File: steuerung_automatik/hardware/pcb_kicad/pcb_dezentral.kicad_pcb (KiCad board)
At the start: 2 copper layers, 55 x 73.5 mm, 84 parts, among them J1 1146810000, J2 1146900000, J901 USB_C_Receptacle_USB2.0, Q1 AO3400A, SW1 dip_switch_SPST16, SW901 SW_MEC_5E, U1 SP3485EN-L/TR, U2 AOZ1282CI, U901 RP2040, U902 AMS1117-3.3, U903 W25Q128JVS, Y901 Crystal_GND24_Small

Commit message: Testpunkte
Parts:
- added D26: LED RED, 00_project_library:LED_0603_1608Metric, F.Cu at (80.3, 99.1)
- added IO18: TestPoint, TestPoint:TestPoint_Pad_D1.0mm, F.Cu at (80.6, 93.1)
- added IO19: TestPoint, TestPoint:TestPoint_Pad_D1.0mm, F.Cu at (80.6, 95.2)
- added IO20: TestPoint, TestPoint:TestPoint_Pad_D1.0mm, F.Cu at (80.5, 97.3)
- added R14: 470R, Resistor_SMD:R_0402_1005Metric_Pad0.72x0.64mm_HandSolder, F.Cu at (78.7, 97.0)
- J1: value 1146810000 -> weidmueller_SL5.08HC-06-90
- J2: value 1146900000 -> weidmueller_SL5.08HC-10-90
- moved R905 39.7 mm to (108.0, 96.4), turned to -90 degrees
- moved D901 34.9 mm to (107.2, 98.5), turned to 180 degrees
- moved C915 2.04 mm to (81.0, 100.5), turned to 180 degrees
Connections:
- U901 pad 29: unconnected-(U901-GPIO18-Pad29) -> Net-(U901-GPIO18)
- U901 pad 30: unconnected-(U901-GPIO19-Pad30) -> Net-(U901-GPIO19)
- U901 pad 31: unconnected-(U901-GPIO20-Pad31) -> Net-(U901-GPIO20)
- U901 pad 32: unconnected-(U901-GPIO21-Pad32) -> modbus_led
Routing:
- net Net-(U901-GPIO18): track 0.00 -> 7.25 mm
- net Net-(U901-GPIO19): track 0.00 -> 5.87 mm
- net Net-(U901-GPIO20): track 0.00 -> 4.27 mm
- net +3V3: track 282.2 -> 279.0 mm
- net modbus_led: track 0.00 -> 2.56 mm
- net Net-(D901-K): track 2.31 -> 0.00 mm
- net Net-(D26-K): track 0.00 -> 1.84 mm
- net ds_5: track 64.9 -> 66.5 mm
- net ds_6: track 68.6 -> 70.3 mm
- net ds_4: track 60.8 -> 62.5 mm
- net ds_2: track 52.2 -> 53.8 mm
- net ds_7: track 72.6 -> 74.3 mm
- net ds_3: track 56.6 -> 58.2 mm
- net ds_1: track 48.6 -> 50.1 mm
- net ds_0: track 47.3 -> 48.2 mm
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
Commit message: pcb_dezentral v0.8
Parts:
- added D27: LED BLUE, 00_project_library:LED_0603_1608Metric, F.Cu at (112.4, 90.0)
- added R15: 470R, Resistor_SMD:R_0402_1005Metric_Pad0.72x0.64mm_HandSolder, F.Cu at (113.0, 88.5)
- added R16: 470R, Resistor_SMD:R_0402_1005Metric_Pad0.72x0.64mm_HandSolder, F.Cu at (108.5, 88.4)
- D17: value SMBJ30A -> LED RED; footprint Diode_SMD:D_SMA -> 00_project_library:LED_0603_1608Metric
- D26: value LED RED -> SMBJ30CA; footprint 00_project_library:LED_0603_1608Metric -> Diode_SMD:D_SMB
- R14: value 470R -> 4k7
- moved D26 37.2 mm to (112.7, 117.3)
- moved D17 27.4 mm to (107.8, 90.1)
- moved R905 4.15 mm to (108.0, 100.6), turned to 90 degrees
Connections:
- C1 pad 1: Net-(D19-K) -> 24Vp
- C2 pad 1: Net-(D19-K) -> 24Vp
- D17 pad 1: 485_24V -> Net-(D17-K)
- D17 pad 2: GND -> MODBUS_DE
- D19 pad 1: Net-(D19-K) -> 24Vp
- D20 pad 1: 485_24V -> 24Vp
- D26 pad 1: Net-(D26-K) -> GND
- D26 pad 2: modbus_led -> 485_24V
- J1 pad 5: 485_24V -> 24Vp
- R11 pad 1: Net-(D19-K) -> 24Vp
- R14 pad 1: GND -> MODBUS_DE
- R14 pad 2: Net-(D26-K) -> GND
- U2 pad 5: Net-(D19-K) -> 24Vp
- U901 pad 32: modbus_led -> unconnected-(U901-GPIO21-Pad32)
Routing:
- net 24Vp: track 0.00 -> 35.3 mm
- net MODBUS_RO: track 14.6 -> 41.0 mm, vias 2 -> 4
- net MODBUS_DE: track 16.6 -> 40.1 mm, vias 0 -> 2
- net Net-(D19-K): track 12.0 -> 0.00 mm
- net 485_24V: track 38.5 -> 33.9 mm
- net +3V3: track 279.0 -> 282.1 mm
- net modbus_led: track 2.56 -> 0.00 mm
- net Net-(D17-K): track 0.00 -> 1.90 mm
- net Net-(D26-K): track 1.84 -> 0.00 mm
- net GND: track 90.9 -> 89.2 mm
- net Net-(D27-A): track 0.00 -> 1.68 mm
- net Net-(D901-K): track 0.00 -> 1.42 mm
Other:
- board text added: "0V"
- board text added: "24V"
- board text added: "3V3"
- board text added: "485"
- board text added: "A"
- board text added: "B"
- board text added: "DS_1"
- board text added: "DS_2"
- board text added: "DS_3"
- board text added: "DS_4"
- board text added: "DS_5"
- board text added: "DS_6"
- board text added: "DS_7"
- board text added: "GND"
- board text added: "MODBUS"
- board text added: "PWR"
- board text added: "RX"
- board text added: "TX"
- board text added: "locked"
- board text added: "rel_n"
- board text added: "rel_p"

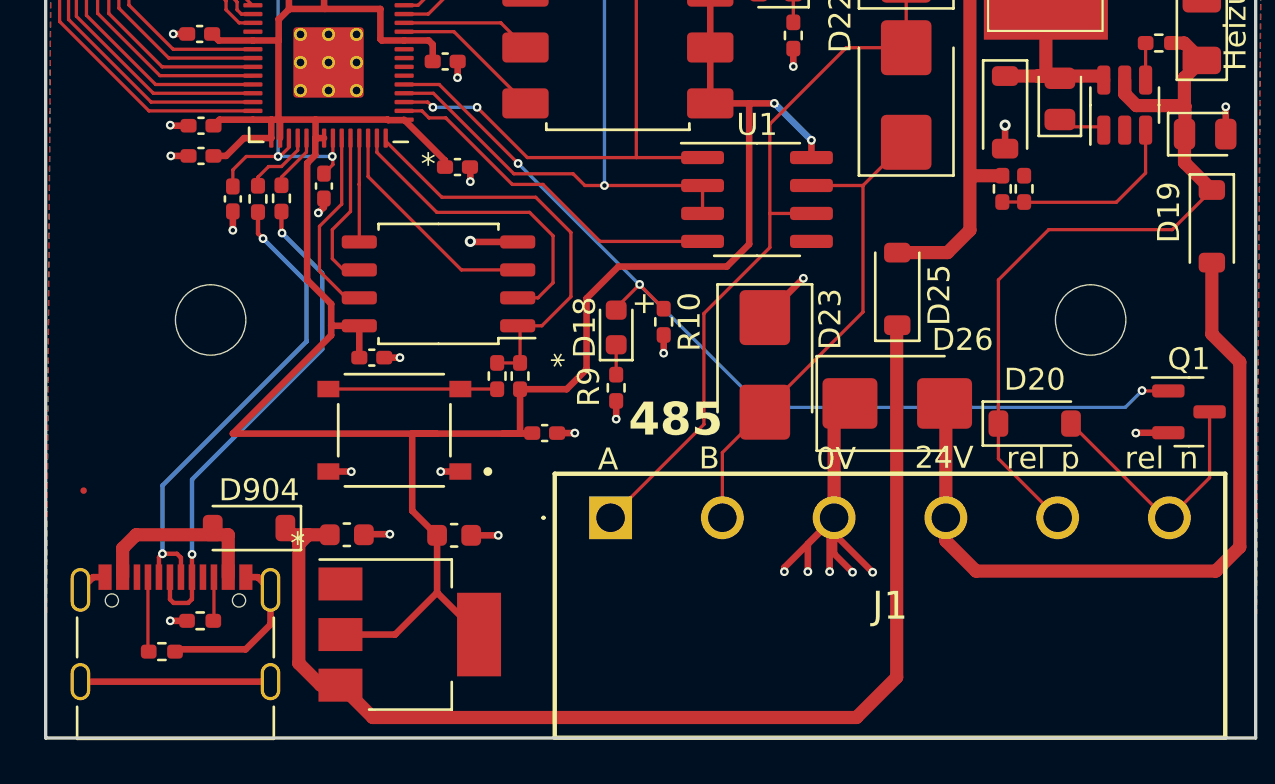
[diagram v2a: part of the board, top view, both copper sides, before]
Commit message: pcb_dezentral, update J1/J2, v0.8
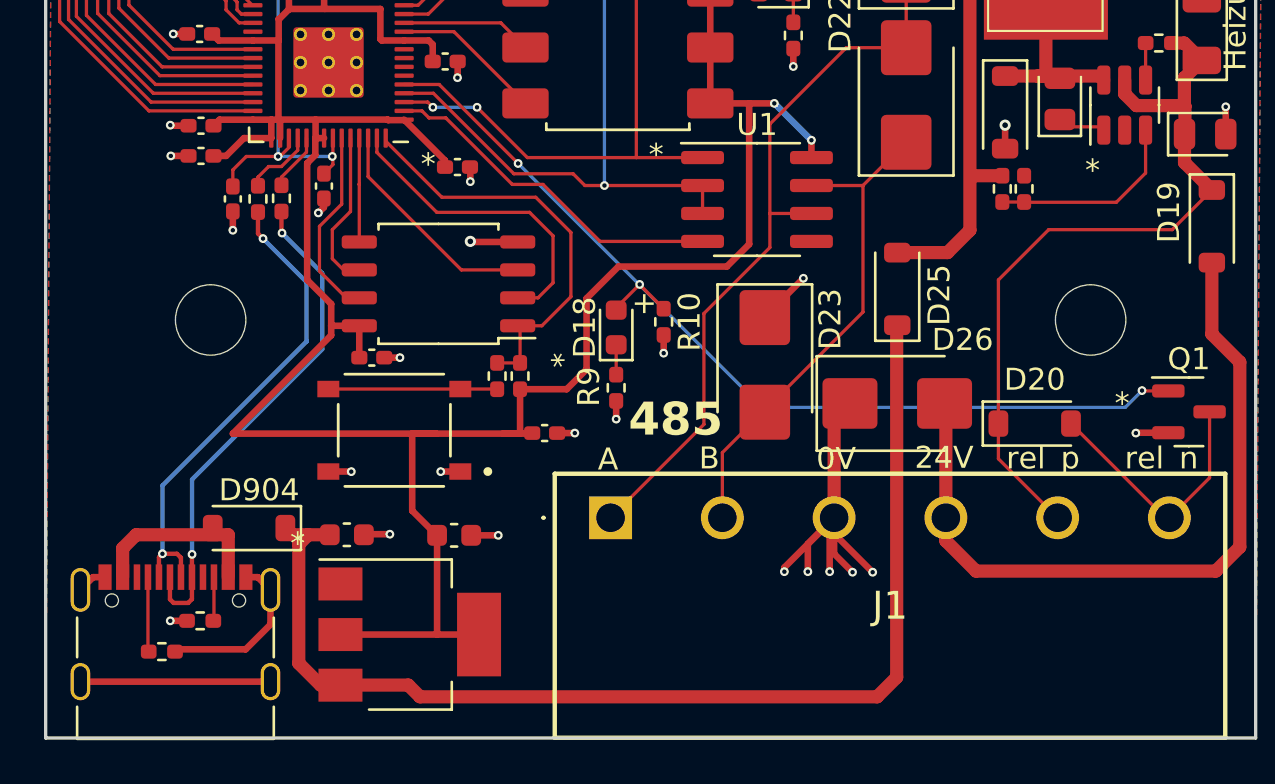
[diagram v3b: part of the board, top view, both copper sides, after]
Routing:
- net +5V: track 53.1 -> 52.3 mm
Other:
- board text added: "*"
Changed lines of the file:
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@@
     (descr "Diode SMD 1206 (3216 Metric), square (rectangular) end terminal, IPC_7351 nominal, (Body size source: http://www.tortai-tech.com/upload/download/2011102023233369053.pdf), generated with kicad-footprint-generator")
     (tags "diode")
-    (property "JLC" "C49678")
+    (property "JLC" "C515689")
     (property "Sheetfile" "pcb_dezentral.kicad_sch")
     (property "Sheetname" "")
@@
     (property "Sheetfile" "pcb_dezentral_cpu.kicad_sch")
     (property "Sheetname" "cpu")
+    (property "exclude_from_bom" "")
     (property "ki_description" "test point")
     (property "ki_keywords" "test point tp")
-    (attr exclude_from_pos_files)
+    (attr exclude_from_pos_files exclude_from_bom)
     (fp_text reference "IO20" (at -4 0) (layer "F.SilkS")
         (effects (font (size 1 1) (thickness 0.15)))
@@
     (property "Sheetfile" "pcb_dezentral_cpu.kicad_sch")
     (property "Sheetname" "cpu")
+    (property "exclude_from_bom" "")
     (property "ki_description" "test point")
     (property "ki_keywords" "test point tp")
-    (attr exclude_from_pos_files)
+    (attr exclude_from_pos_files exclude_from_bom)
     (fp_text reference "IO19" (at -4.1 0.2) (layer "F.SilkS")
         (effects (font (size 1 1) (thickness 0.15)))
@@
     (property "Arrow Price/Stock" "")
     (property "Height" "8.4")
+    (property "JLC" "C46026")
     (property "Manufacturer_Name" "Weidmuller")
     (property "Manufacturer_Part_Number" "1146900000")
@@
     (property "Arrow Price/Stock" "")
     (property "Height" "8.4")
+    (property "JLC" "C8472")
     (property "Manufacturer_Name" "Weidmuller")
     (property "Manufacturer_Part_Number" "1146810000")
@@
     (property "Sheetfile" "pcb_dezentral_cpu.kicad_sch")
     (property "Sheetname" "cpu")
+    (property "exclude_from_bom" "")
     (property "ki_description" "test point")
     (property "ki_keywords" "test point tp")
-    (attr exclude_from_pos_files)
+    (attr exclude_from_pos_files exclude_from_bom)
     (fp_text reference "IO18" (at -4.1 0.1) (layer "F.SilkS")
         (effects (font (size 1 1) (thickness 0.15)))
@@
     (effects (font (size 1 1) (thickness 0.15)) (justify left bottom))
   )
+  (gr_text "*" (at 121.2438 107.2874) (layer "F.SilkS")
+    (effects (font (size 1 1) (thickness 0.15)) (justify left bottom))
+  )
   (gr_text "PWR" (at 108.6826 97.8148 90) (layer "F.SilkS")
     (effects (font (size 1.5 1.5) (thickness 0.3) bold) (justify left bottom))
@@
     (effects (font (size 1.5 1.5) (thickness 0.3) bold) (justify left bottom))
   )
+  (gr_text "*" (at 122.59 117.8792) (layer "F.SilkS")
+    (effects (font (size 1 1) (thickness 0.15)) (justify left bottom))
+  )
   (gr_text "rel_p" (at 117.6624 120.3684) (layer "F.SilkS")
     (effects (font (size 1 1) (thickness 0.15)) (justify left bottom))
@@
     (effects (font (size 1.5 1.5) (thickness 0.3) bold) (justify left bottom))
   )
+  (gr_text "*" (at 101.4064 106.5762) (layer "F.SilkS")
+    (effects (font (size 1 1) (thickness 0.15)) (justify left bottom))
+  )
   (gr_text "B" (at 103.6924 120.3684) (layer "F.SilkS")
     (effects (font (size 1 1) (thickness 0.15)) (justify left bottom))
@@
     (effects (font (size 1.5 1.5) (thickness 0.3) bold) (justify left bottom))
   )
-  (segment (start 112.684 113.7634) (end 112.684 129.741) (width 0.6) (layer "F.Cu") (net 1))
+  (segment (start 90.4844 130.0966) (end 87.4034 130.0966) (width 0.6) (layer "F.Cu") (net 1))
+  (segment (start 91.0178 130.63) (end 90.4844 130.0966) (width 0.6) (layer "F.Cu") (net 1))
+  (segment (start 111.795 130.63) (end 91.0178 130.63) (width 0.6) (layer "F.Cu") (net 1))
   (segment (start 87.4 130.1) (end 86.5 130.1) (width 0.6) (layer "F.Cu") (net 1))
   (segment (start 85.506 123.6958) (end 85.9378 123.264) (width 0.6) (layer "F.Cu") (net 1))
   (segment (start 85.9378 123.264) (end 85.2002 123.264) (width 0.6) (layer "F.Cu") (net 1))
+  (segment (start 112.684 113.7634) (end 112.684 129.741) (width 0.6) (layer "F.Cu") (net 1))
   (segment (start 85.506 129.106) (end 85.506 123.6958) (width 0.6) (layer "F.Cu") (net 1))
-  (segment (start 112.684 129.741) (end 110.8552 131.5698) (width 0.6) (layer "F.Cu") (net 1))
   (segment (start 85.9378 123.264) (end 86.9154 123.264) (width 0.6) (layer "F.Cu") (net 1))
-  (segment (start 88.8698 131.5698) (end 87.4 130.1) (width 0.6) (layer "F.Cu") (net 1))
   (segment (start 86.5 130.1) (end 85.506 129.106) (width 0.6) (layer "F.Cu") (net 1))
-  (segment (start 110.8552 131.5698) (end 88.8698 131.5698) (width 0.6) (layer "F.Cu") (net 1))
   (segment (start 85.2002 123.264) (end 84.8954 122.9592) (width 0.6) (layer "F.Cu") (net 1))
+  (segment (start 112.684 129.741) (end 111.795 130.63) (width 0.6) (layer "F.Cu") (net 1))
   (segment (start 83.1184 106.0682) (end 84.5662 106.0682) (width 0.15) (layer "F.Cu") (net 2))
   (segment (start 85.0572 105.660522) (end 85.0572 105.2335) (width 0.15) (layer "F.Cu") (net 2))
@@
   (segment (start 86.7131 81.3042) (end 86.7131 80.2638) (width 0.3) (layer "F.Cu") (net 8))
   (segment (start 127.6413 105.0522) (end 127.6413 103.8109) (width 0.3) (layer "F.Cu") (net 8))
-  (segment (start 75.7258 121.2562) (end 75.727 121.2574) (width 0.3) (layer "F.Cu") (net 8))
   (segment (start 91.9622 120.3892) (end 91.9576 120.3938) (width 0.3) (layer "F.Cu") (net 8))
   (segment (start 87.8572 98.3585) (end 87.8572 97.4432) (width 0.3) (layer "F.Cu") (net 8))
@@
   (segment (start 83.4197 104.396) (end 81.9037 104.396) (width 0.3) (layer "F.Cu") (net 16))
   (segment (start 90.2947 104.396) (end 92.1521 106.2534) (width 0.3) (layer "F.Cu") (net 16))
-  (segment (start 91.7922 125.8922) (end 93.7 127.8) (width 0.3) (layer "F.Cu") (net 16))
   (segment (start 84.2572 105.2335) (end 83.0133 105.2335) (width 0.3) (layer "F.Cu") (net 16))
   (segment (start 84.5806 104.3342) (end 84.6424 104.396) (width 0.3) (layer "F.Cu") (net 16))
@@
   (segment (start 112.0877 66.3954) (end 112.0623 66.37) (width 0.3) (layer "F.Cu") (net 16))
   (segment (start 79.9313 73.3925) (end 81.5204 73.3925) (width 0.3) (layer "F.Cu") (net 16))
+  (segment (start 91.7922 123.2894) (end 91.7922 127.8) (width 0.3) (layer "F.Cu") (net 16))
   (segment (start 112.3525 88.466) (end 112.3525 87.1439) (width 0.3) (layer "F.Cu") (net 16))
   (segment (start 105.9784 103.6552) (end 104.2094 103.6552) (width 0.3) (layer "F.Cu") (net 16))
@@
   (segment (start 84.5806 100.796) (end 84.5806 104.3342) (width 0.3) (layer "F.Cu") (net 16))
   (segment (start 104.2094 98.5752) (end 106.3847 98.5752) (width 0.3) (layer "F.Cu") (net 16))
-  (segment (start 87.4 127.8) (end 89.8844 127.8) (width 0.3) (layer "F.Cu") (net 16))
   (segment (start 83.4197 100.796) (end 81.8635 100.796) (width 0.3) (layer "F.Cu") (net 16))
   (segment (start 90.2947 100.796) (end 91.4098 100.796) (width 0.3) (layer "F.Cu") (net 16))
@@
   (segment (start 95.5644 118.6412) (end 95.5644 116.6479) (width 0.3) (layer "F.Cu") (net 16))
   (segment (start 85.887 106.373) (end 85.887 111.6816) (width 0.3) (layer "F.Cu") (net 16))
+  (segment (start 91.7922 127.8) (end 93.7 127.8) (width 0.3) (layer "F.Cu") (net 16))
   (segment (start 91.5933 100.9795) (end 91.5933 101.7502) (width 0.3) (layer "F.Cu") (net 16))
   (segment (start 104.2094 103.6552) (end 104.2094 85.8752) (width 0.3) (layer "F.Cu") (net 16))
@@
   (segment (start 96.7969 66.4462) (end 96.8731 66.37) (width 0.3) (layer "F.Cu") (net 16))
   (segment (start 86.268 105.2227) (end 86.268 104.3918) (width 0.3) (layer "F.Cu") (net 16))
-  (segment (start 91.7922 123.2894) (end 91.7922 125.8922) (width 0.3) (layer "F.Cu") (net 16))
   (segment (start 84.9605 73.3417) (end 86.6258 73.3417) (width 0.3) (layer "F.Cu") (net 16))
   (segment (start 94.8024 118.6666) (end 96.0891 118.6666) (width 0.3) (layer "F.Cu") (net 16))
@@
   (segment (start 84.2572 104.4002) (end 84.2614 104.396) (width 0.3) (layer "F.Cu") (net 16))
   (segment (start 89.57 104.4172) (end 89.5446 104.3918) (width 0.3) (layer "F.Cu") (net 16))
+  (segment (start 87.4 127.8) (end 91.7922 127.8) (width 0.3) (layer "F.Cu") (net 16))
   (segment (start 96.7969 73.3052) (end 96.7969 66.4462) (width 0.3) (layer "F.Cu") (net 16))
   (segment (start 98.587 112.5198) (end 98.587 115.7456) (width 0.3) (layer "F.Cu") (net 16))
@@
   (segment (start 98.587 115.7456) (end 97.6847 116.6479) (width 0.3) (layer "F.Cu") (net 16))
   (segment (start 84.6466 104.3918) (end 84.6424 104.396) (width 0.3) (layer "F.Cu") (net 16))
-  (segment (start 89.8844 127.8) (end 91.7922 125.8922) (width 0.3) (layer "F.Cu") (net 16))
   (segment (start 84.6572 104.4108) (end 84.6424 104.396) (width 0.3) (layer "F.Cu") (net 16))
   (segment (start 94.8024 118.6666) (end 95.539 118.6666) (width 0.3) (layer "F.Cu") (net 16))
